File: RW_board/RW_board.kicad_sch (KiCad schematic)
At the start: 2 parts, among them J3 1-84953-1, J4 Conn_01x06_Pin

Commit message: Fixed text
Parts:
- removed J4: Conn_01x06_Pin, Connector_Molex:Molex_PicoBlade_53048-0610_1x06_P1.25mm_Horizontal, symbol Connector:Conn_01x06_Pin
- added J4: Conn_01x08_Pin, Connector_Molex:Molex_PicoBlade_53048-0810_1x08_P1.25mm_Horizontal, symbol Connector:Conn_01x08_Pin
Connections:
- net GND: now also J4.3 (Pin_3), J4.4 (Pin_4)
- net RX: now also J4.6 (Pin_6)
- net TX: now also J4.5 (Pin_5)
- net VDC: now also J4.1 (Pin_1), J4.2 (Pin_2)
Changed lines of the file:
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@@
 	)
 	(symbol
-		(lib_id "Connector:Conn_01x06_Pin")
-		(at 29.21 163.83 0)
+		(lib_id "Connector:Conn_01x08_Pin")
+		(at 29.21 166.37 0)
 		(unit 1)
 		(exclude_from_sim no)
@@
 			)
 		)
-		(property "Value" "Conn_01x06_Pin"
+		(property "Value" "Conn_01x08_Pin"
 			(at 29.845 156.21 0)
 			(effects
@@
 			)
 		)
-		(property "Footprint" "Connector_Molex:Molex_PicoBlade_53048-0610_1x06_P1.25mm_Horizontal"
-			(at 29.21 163.83 0)
+		(property "Footprint" "Connector_Molex:Molex_PicoBlade_53048-0810_1x08_P1.25mm_Horizontal"
+			(at 29.21 166.37 0)
 			(effects
 				(font
@@
 		)
 		(property "Datasheet" "~"
-			(at 29.21 163.83 0)
+			(at 29.21 166.37 0)
 			(effects
 				(font
@@
 			)
 		)
-		(property "Description" "Generic connector, single row, 01x06, script generated"
-			(at 29.21 163.83 0)
+		(property "Description" "Generic connector, single row, 01x08, script generated"
+			(at 29.21 166.37 0)
 			(effects
 				(font
@@
 			)
 		)
+		(pin "4"
+		)
+		(pin "1"
+		)
 		(pin "6"
 		)
-		(pin "4"
+		(pin "8"
 		)
 		(pin "2"
 		)
+		(pin "5"
+		)
+		(pin "7"
+		)
 		(pin "3"
 		)
-		(pin "5"
-		)
-		(pin "1"
-		)
 		(instances

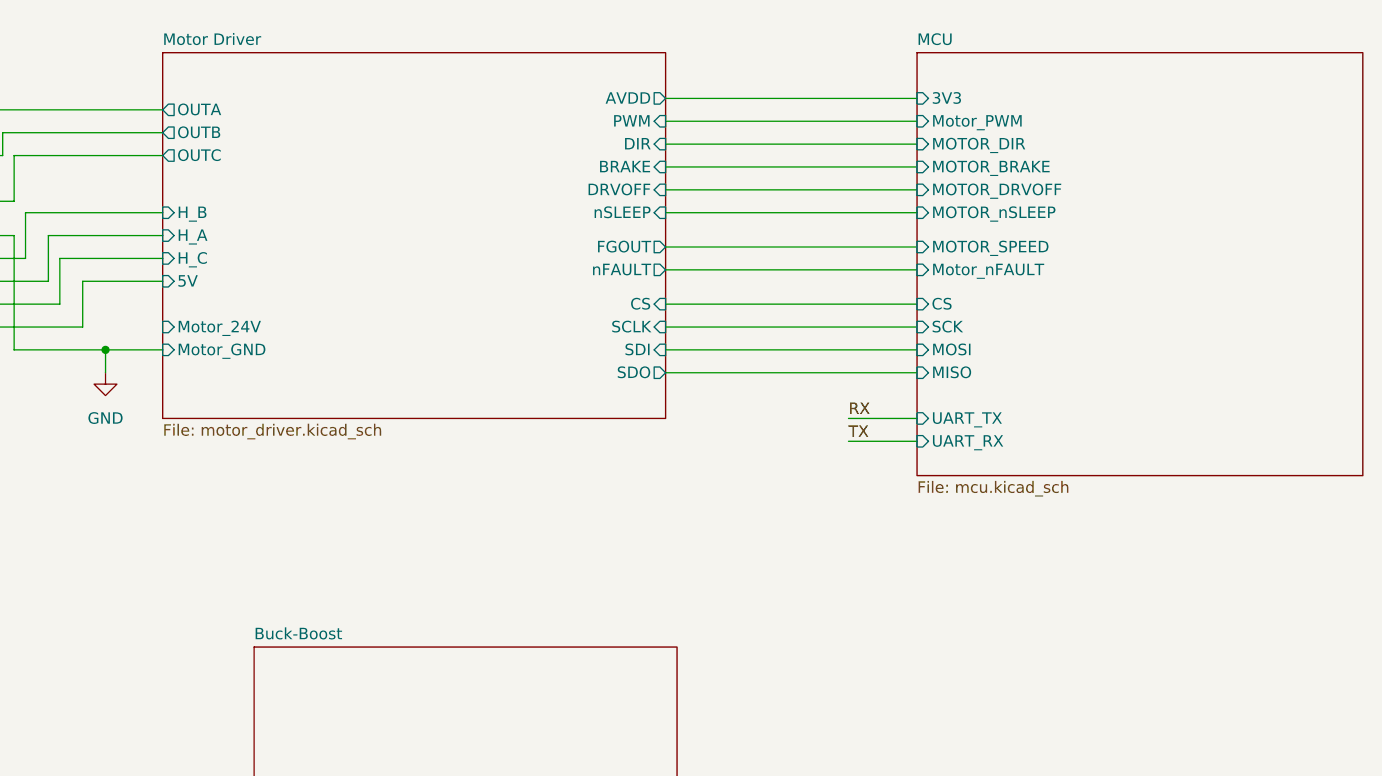
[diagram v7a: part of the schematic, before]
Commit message: Added ADC inputs
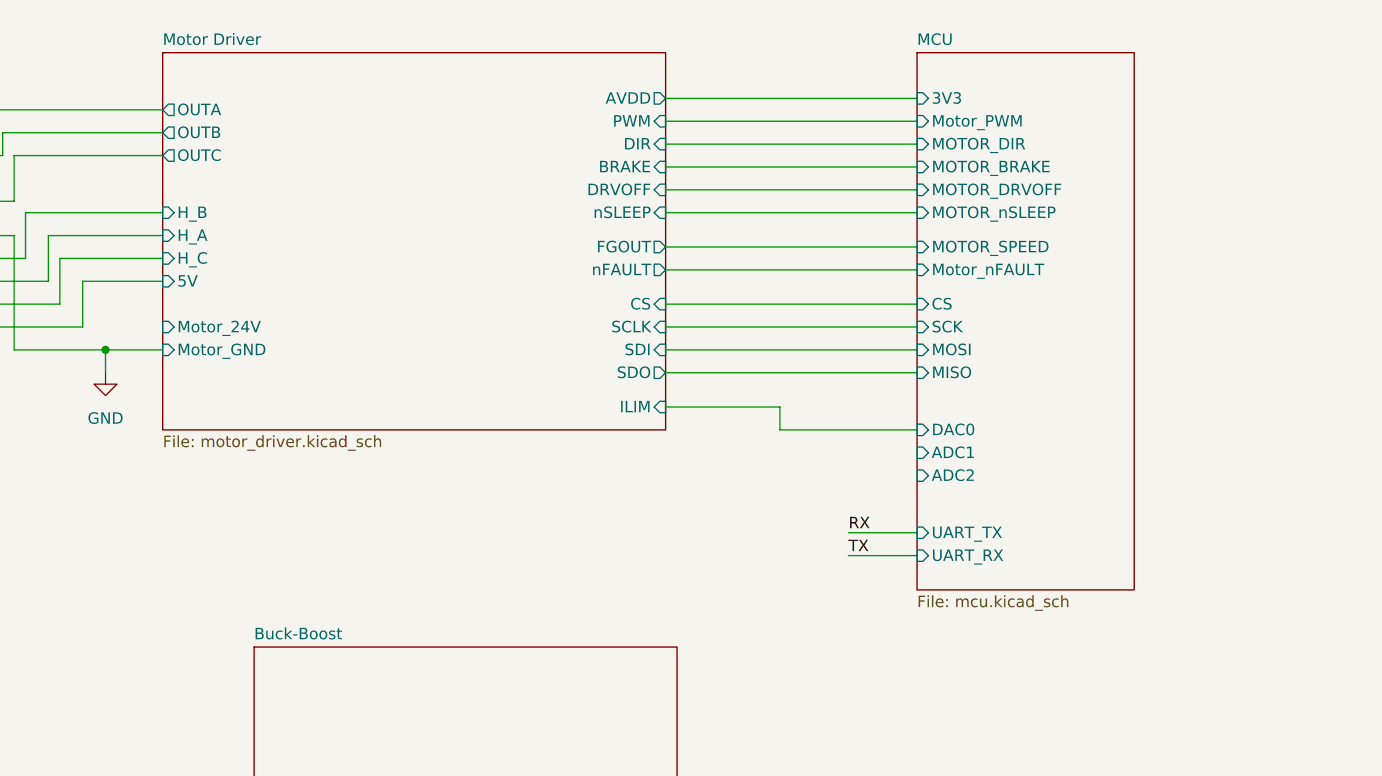
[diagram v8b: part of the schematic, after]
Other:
- sheet MCU ports: added ADC1, ADC2, DAC0; removed none
- sheet Motor Driver ports: added ILIM; removed none
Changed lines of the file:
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@@
+	(wire
+		(pts
+			(xy 156.21 105.41) (xy 171.45 105.41)
+		)
+		(stroke
+			(width 0)
+			(type default)
+		)
+	)
 	(wire
 		(pts
@@
 	(wire
 		(pts
+			(xy 143.51 102.87) (xy 156.21 102.87)
+		)
+		(stroke
+			(width 0)
+			(type default)
+		)
+	)
+	(wire
+		(pts
 			(xy 34.29 171.45) (xy 39.37 171.45)
 		)
@@
 	(wire
 		(pts
-			(xy 163.83 104.14) (xy 171.45 104.14)
+			(xy 163.83 116.84) (xy 171.45 116.84)
 		)
 		(stroke
@@
 	(wire
 		(pts
-			(xy 163.83 106.68) (xy 171.45 106.68)
+			(xy 163.83 119.38) (xy 171.45 119.38)
 		)
 		(stroke
@@
 		(pts
 			(xy 87.63 88.9) (xy 78.74 88.9)
+		)
+		(stroke
+			(width 0)
+			(type default)
+		)
+	)
+	(wire
+		(pts
+			(xy 156.21 102.87) (xy 156.21 105.41)
 		)
 		(stroke
@@
 	)
 	(label "TX"
-		(at 163.83 106.68 0)
+		(at 163.83 119.38 0)
 		(effects
 			(font
@@
 	)
 	(label "RX"
-		(at 163.83 104.14 0)
+		(at 163.83 116.84 0)
 		(effects
 			(font
@@
 	(sheet
 		(at 87.63 63.5)
-		(size 55.88 40.64)
+		(size 55.88 41.91)
 		(fields_autoplaced yes)
 		(stroke
@@
 		)
 		(property "Sheetfile" "motor_driver.kicad_sch"
-			(at 87.63 104.7246 0)
+			(at 87.63 105.9946 0)
 			(effects
 				(font
@@
 				)
 				(justify left)
+			)
+		)
+		(pin "ILIM" input
+			(at 143.51 102.87 0)
+			(effects
+				(font
+					(size 1.27 1.27)
+				)
+				(justify right)
 			)
 		)
@@
 	(sheet
 		(at 171.45 63.5)
-		(size 49.53 46.99)
+		(size 24.13 59.69)
 		(fields_autoplaced yes)
 		(stroke
@@
 		)
 		(property "Sheetfile" "mcu.kicad_sch"
-			(at 171.45 111.0746 0)
+			(at 171.45 123.7746 0)
 			(effects
 				(font
@@
 		)
 		(pin "UART_TX" input
-			(at 171.45 104.14 180)
+			(at 171.45 116.84 180)
 			(effects
 				(font
@@
 		)
 		(pin "UART_RX" input
-			(at 171.45 106.68 180)
-			(effects
-				(font
+			(at 171.45 119.38 180)
+			(effects
+				(font
+					(size 1.27 1.27)
+				)
+				(justify left)
+			)
+		)
+		(pin "ADC1" input
+			(at 171.45 107.95 180)
+			(effects
+				(font
+					(size 1.27 1.27)
+				)
+				(justify left)
+			)
+		)
+		(pin "ADC2" input
+			(at 171.45 110.49 180)
+			(effects
+				(font
+					(size 1.27 1.27)
+				)
+				(justify left)
+			)
+		)
+		(pin "DAC0" input
+			(at 171.45 105.41 180)
+			(effects
+				(font
